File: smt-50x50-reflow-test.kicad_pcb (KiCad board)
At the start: 4 copper layers, 0 parts

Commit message: pcb: fix missing 3d models
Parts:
- added AE1: Antenna, RF_Antenna:Johanson_2450AT18x100, F.Cu at (162.5, 82.0)
- added C1: 1u, Capacitor_SMD:C_0603_1608Metric, F.Cu at (128.3, 74.4)
- added C10: 0u1, Capacitor_SMD:C_0402_1005Metric, F.Cu at (127.7, 95.6)
- added C11: 0u1, Capacitor_SMD:C_0402_1005Metric, F.Cu at (127.7, 97.6)
- added C12: 0u1, Capacitor_SMD:C_0402_1005Metric, F.Cu at (127.7, 99.5)
- added C13: 10n, Capacitor_SMD:C_0402_1005Metric, F.Cu at (127.7, 101.5)
- added C14: 1u, Capacitor_SMD:C_0402_1005Metric, F.Cu at (130.6, 91.7)
- added C15: 1u, Capacitor_SMD:C_0402_1005Metric, F.Cu at (130.6, 93.6)
- added C16: 0u1, Capacitor_SMD:C_0402_1005Metric, F.Cu at (130.6, 95.6)
- added C17: 0u1, Capacitor_SMD:C_0402_1005Metric, F.Cu at (130.6, 97.6)
- added C18: 0u1, Capacitor_SMD:C_0402_1005Metric, F.Cu at (130.6, 99.5)
- added C19: 1u, Capacitor_SMD:C_0402_1005Metric, F.Cu at (130.6, 101.5)
- added C2: 1u, Capacitor_SMD:C_0603_1608Metric, F.Cu at (128.3, 76.9)
- added C20: 10u, Capacitor_SMD:C_0402_1005Metric, F.Cu at (133.5, 91.7)
- added C21: 22u, Capacitor_SMD:C_0603_1608Metric, F.Cu at (128.3, 84.4)
- added C22: 1u, Capacitor_SMD:C_0402_1005Metric, F.Cu at (133.5, 93.6)
- added C23: 12p, Capacitor_SMD:C_0402_1005Metric, F.Cu at (133.5, 95.6)
- added C25: 12p, Capacitor_SMD:C_0402_1005Metric, F.Cu at (133.5, 97.6)
- added C28: 1p2, Capacitor_SMD:C_0402_1005Metric, F.Cu at (133.5, 99.5)
- added C29: 1p2, Capacitor_SMD:C_0402_1005Metric, F.Cu at (133.5, 101.5)
- added C4: 0u1, Capacitor_SMD:C_0603_1608Metric, F.Cu at (128.3, 79.4)
- added C48: 0u1, Capacitor_SMD:C_0402_1005Metric, F.Cu at (136.4, 91.7)
- added C49: 0u1, Capacitor_SMD:C_0402_1005Metric, F.Cu at (136.4, 93.6)
- added C5: 1u, Capacitor_SMD:C_0603_1608Metric, F.Cu at (128.3, 81.9)
- added C50: 0u1, Capacitor_SMD:C_0402_1005Metric, F.Cu at (136.4, 95.6)
- added C51: 0u1, Capacitor_SMD:C_0402_1005Metric, F.Cu at (136.4, 97.6)
- added C52: 1p, Capacitor_SMD:C_0402_1005Metric, F.Cu at (136.4, 99.5)
- added C6: 4u7, Capacitor_SMD:C_1206_3216Metric, F.Cu at (141.2, 109.2)
- added C7: 4u7, Capacitor_SMD:C_1206_3216Metric, F.Cu at (141.2, 112.5)
- added C8: 10u, Capacitor_SMD:C_0402_1005Metric, F.Cu at (127.7, 91.7)
- added C9: 1u, Capacitor_SMD:C_0402_1005Metric, F.Cu at (127.7, 93.6)
- added D1: RED, LED_SMD:LED_0603_1608Metric, F.Cu at (165.8, 110.0)
- added D2: GREEN, LED_SMD:LED_0805_2012Metric, F.Cu at (160.9, 112.2)
- added D3: H5VU10U, Pers:Diode_DFN1006, F.Cu at (152.8, 82.3)
- added D5: WHITE, LED_SMD:LED_0603_1608Metric, F.Cu at (165.8, 112.6)
- added D7: D_Schottky, Diode_SMD:D_SMA, F.Cu at (142.4, 105.2)
- added J1: Conn_01x04_Pin, Connector_PinHeader_2.54mm:PinHeader_1x04_P2.54mm_Vertical, F.Cu at (140.6, 75.4)
- added J2: Conn_01x02, Connector_PinHeader_2.54mm:PinHeader_1x02_P2.54mm_Vertical, F.Cu at (162.0, 75.4)
- added J4: USB_C_Receptacle_USB2.0_14P, Connector_USB:USB_C_Receptacle_HRO_TYPE-C-31-M-12, F.Cu at (132.2, 108.3)
- added J8: Conn_01x04_Pin, Connector_PinHeader_2.54mm:PinHeader_1x04_P2.54mm_Vertical, F.Cu at (145.2, 75.4)
- added J9: Conn_01x03_Pin, Connector_PinHeader_2.54mm:PinHeader_1x03_P2.54mm_Vertical, F.Cu at (140.6, 95.6)
- added JP2: Jumper_3_Bridged12, Connector_PinHeader_2.54mm:PinHeader_1x03_P2.54mm_Vertical, F.Cu at (145.2, 95.6)
- added L1: 33u, Inductor_SMD:L_Chilisin_BMRx00060630, F.Cu at (152.5, 97.3)
- added L2: 2n7, Inductor_SMD:L_0402_1005Metric, F.Cu at (139.8, 86.3)
- added L3: 24n, Inductor_SMD:L_0402_1005Metric, F.Cu at (139.8, 88.3)
- added L4: 2n7, Inductor_SMD:L_0402_1005Metric, F.Cu at (139.8, 90.3)
- added L6: 3n9, Inductor_SMD:L_0402_1005Metric, F.Cu at (139.8, 92.3)
- added L7: 2n7, Inductor_SMD:L_0402_1005Metric, F.Cu at (142.7, 86.3)
- added R1: 0, Resistor_SMD:R_0402_1005Metric, F.Cu at (142.7, 88.3)
- added R10: 22, Resistor_SMD:R_0402_1005Metric, F.Cu at (148.5, 88.3)
- added R11: 5k1, Resistor_SMD:R_0603_1608Metric, F.Cu at (128.3, 89.4)
- added R12: 5k1, Resistor_SMD:R_0603_1608Metric, F.Cu at (132.3, 74.4)
- added R13: 5k1, Resistor_SMD:R_0603_1608Metric, F.Cu at (132.3, 76.9)
- added R14: 22, Resistor_SMD:R_0402_1005Metric, F.Cu at (148.5, 90.3)
- added R15: 5k1, Resistor_SMD:R_0603_1608Metric, F.Cu at (132.3, 79.4)
- added R16: 470, Resistor_SMD:R_0402_1005Metric, F.Cu at (148.5, 92.3)
- added R2: 0, Resistor_SMD:R_0402_1005Metric, F.Cu at (142.7, 90.3)
- added R29: 15k, Resistor_SMD:R_0603_1608Metric, F.Cu at (132.3, 81.9)
- added R3: 0, Resistor_SMD:R_0402_1005Metric, F.Cu at (142.7, 92.3)
- added R30: 9k1, Resistor_SMD:R_0603_1608Metric, F.Cu at (132.3, 84.4)
- added R31: 5k1, Resistor_SMD:R_0603_1608Metric, F.Cu at (132.3, 86.9)
- added R32: 100k, Resistor_SMD:R_0603_1608Metric, F.Cu at (132.3, 89.4)
- added R33: 40k, Resistor_SMD:R_0603_1608Metric, F.Cu at (136.3, 74.4)
- added R4: 0, Resistor_SMD:R_0402_1005Metric, F.Cu at (145.6, 86.3)
- added R5: 0, Resistor_SMD:R_0402_1005Metric, F.Cu at (145.6, 88.3)
- added R57: 10k, Resistor_SMD:R_0603_1608Metric, F.Cu at (136.3, 76.9)
- added R58: 10k, Resistor_SMD:R_0603_1608Metric, F.Cu at (136.3, 79.4)
- added R6: 0, Resistor_SMD:R_0402_1005Metric, F.Cu at (145.6, 90.3)
- added R62: 10k, Resistor_SMD:R_0603_1608Metric, F.Cu at (136.3, 81.9)
- added R7: 10k, Resistor_SMD:R_0402_1005Metric, F.Cu at (145.6, 92.3)
- added R8: 10k, Resistor_SMD:R_0402_1005Metric, F.Cu at (148.5, 86.3)
- added R9: 10k, Resistor_SMD:R_0603_1608Metric, F.Cu at (128.3, 86.9)
- added SW1: SW_Push, Button_Switch_SMD:SW_SPST_TS-1088-xR020, F.Cu at (155.1, 103.7)
- added SW2: SW_Push, Button_Switch_SMD:SW_SPST_TS-1088-xR020, F.Cu at (155.1, 108.2)
- added TP13: TestPoint, TestPoint:TestPoint_Pad_D2.0mm, F.Cu at (149.5, 103.5)
- added TP15: TestPoint, TestPoint:TestPoint_Pad_D2.0mm, F.Cu at (149.5, 107.5)
- added TP17: TestPoint, TestPoint:TestPoint_Pad_D2.0mm, F.Cu at (149.5, 111.5)
- added U1: ESP32-C6, Package_DFN_QFN:QFN-40-1EP_5x5mm_P0.4mm_EP3.6x3.6mm_ThermalVias, F.Cu at (163.4, 88.9)
- added U14: TMP117AIDRV, Package_SON:WSON-6-1EP_2x2mm_P0.65mm_EP1x1.6mm, F.Cu at (165.6, 103.3)
- added U15: BMP581, Pers:Bosch_LGA-10_2x2mm_P0.8mm_AntiClockwisePinNumbering, F.Cu at (149.3, 83.2)
- added U16: TMP117AIDRV, Package_SON:WSON-6-1EP_2x2mm_P0.65mm_EP1x1.6mm, F.Cu at (165.6, 106.9)
- added U2: W25Q128JVS, Package_SO:SOIC-8_5.3x5.3mm_P1.27mm, F.Cu at (162.6, 96.8)
- added U3: AP2112K-3.3, Package_TO_SOT_SMD:SOT-23-5, F.Cu at (161.2, 103.8)
- added U4: LM317_TO-252, Package_TO_SOT_SMD:TO-252-2, F.Cu at (154.4, 77.3)
- added U5: LMR36520FADDA, Package_SO:Texas_HTSOP-8-1EP_3.9x4.9mm_P1.27mm_EP2.95x4.9mm_Mask2.4x3.1mm_ThermalVias, F.Cu at (154.7, 88.7)
- added U7: USBLC6-2SC6, Package_TO_SOT_SMD:SOT-23-6, F.Cu at (161.2, 108.5)
- added Y1: 48M, Crystal:Crystal_SMD_2016-4Pin_2.0x1.6mm, F.Cu at (153.6, 112.3)

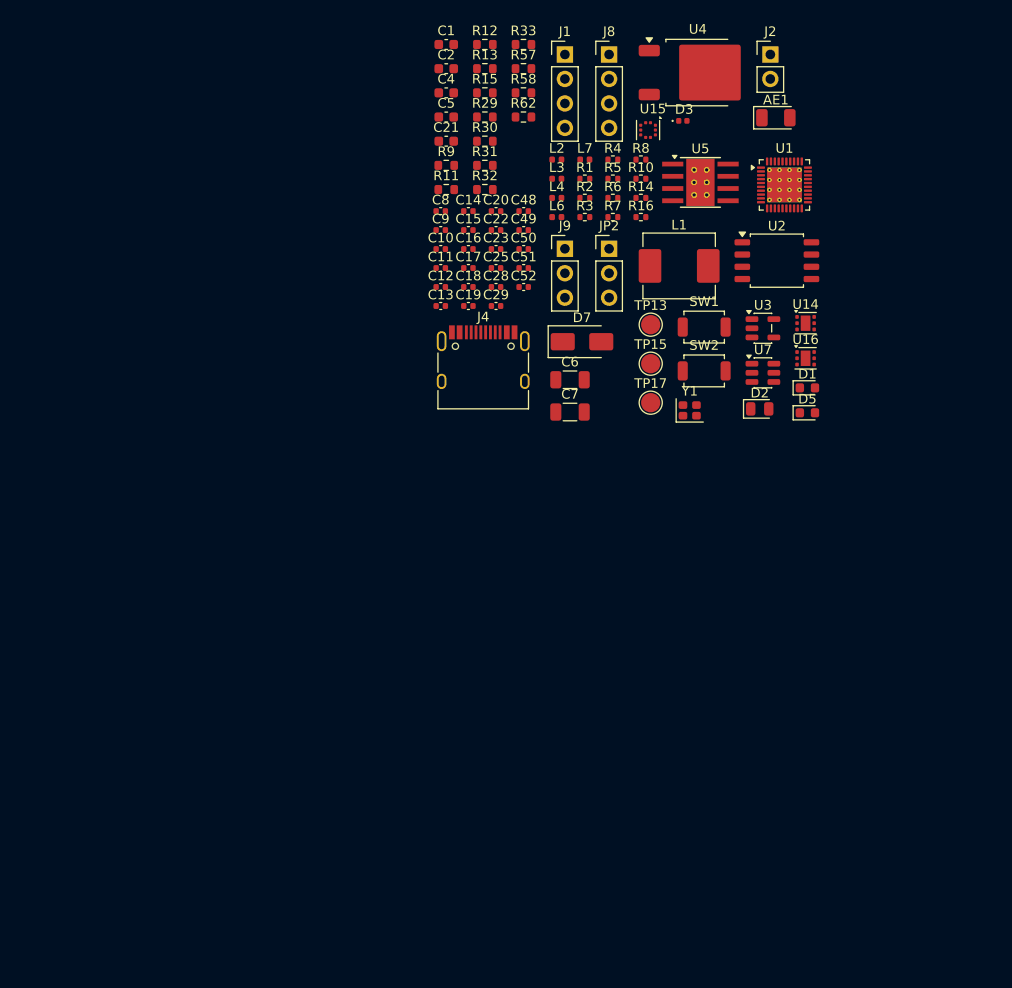
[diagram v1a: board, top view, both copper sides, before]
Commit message: pcb: add board outline
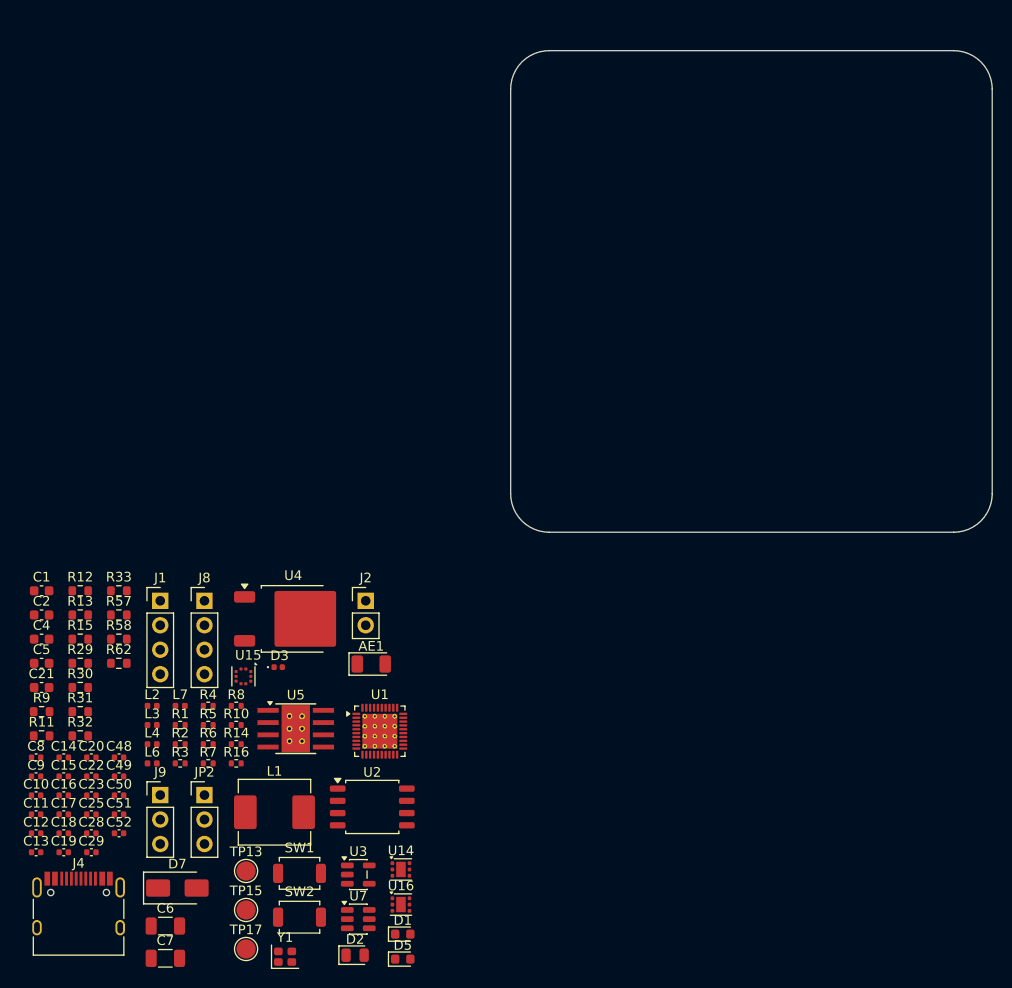
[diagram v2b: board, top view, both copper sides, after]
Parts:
- moved C14 70.6 mm to (88.6, 148.4)
- moved C15 70.6 mm to (88.6, 150.3)
- moved C16 70.6 mm to (88.6, 152.3)
- moved C17 70.6 mm to (88.6, 154.3)
- moved D2 70.6 mm to (118.8, 168.9)
- moved R33 70.6 mm to (94.3, 131.1)
- moved R4 70.6 mm to (103.6, 143.0)
- moved R5 70.6 mm to (103.6, 145.0)
- moved R57 70.6 mm to (94.3, 133.6)
- moved R58 70.6 mm to (94.3, 136.1)
- moved R62 70.6 mm to (94.3, 138.6)
- moved R7 70.6 mm to (103.6, 149.0)
- moved U15 70.6 mm to (107.3, 140.0)
- moved U2 70.6 mm to (120.6, 153.5)
- moved C1 70.6 mm to (86.3, 131.1)
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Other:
- board outline added: 50 x 50 mm

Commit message: pcb: add M2 mounting holes
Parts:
- added REF**: MountingHole_2.2mm_M2_Pad_Via, MountingHole:MountingHole_2.2mm_M2_Pad_Via, F.Cu at (139.0, 121.0)
- added REF**: MountingHole_2.2mm_M2_Pad_Via, MountingHole:MountingHole_2.2mm_M2_Pad_Via, F.Cu at (181.0, 121.0)
- added REF**: MountingHole_2.2mm_M2_Pad_Via, MountingHole:MountingHole_2.2mm_M2_Pad_Via, F.Cu at (181.0, 79.0)
- added REF**: MountingHole_2.2mm_M2_Pad_Via, MountingHole:MountingHole_2.2mm_M2_Pad_Via, F.Cu at (139.0, 79.0)

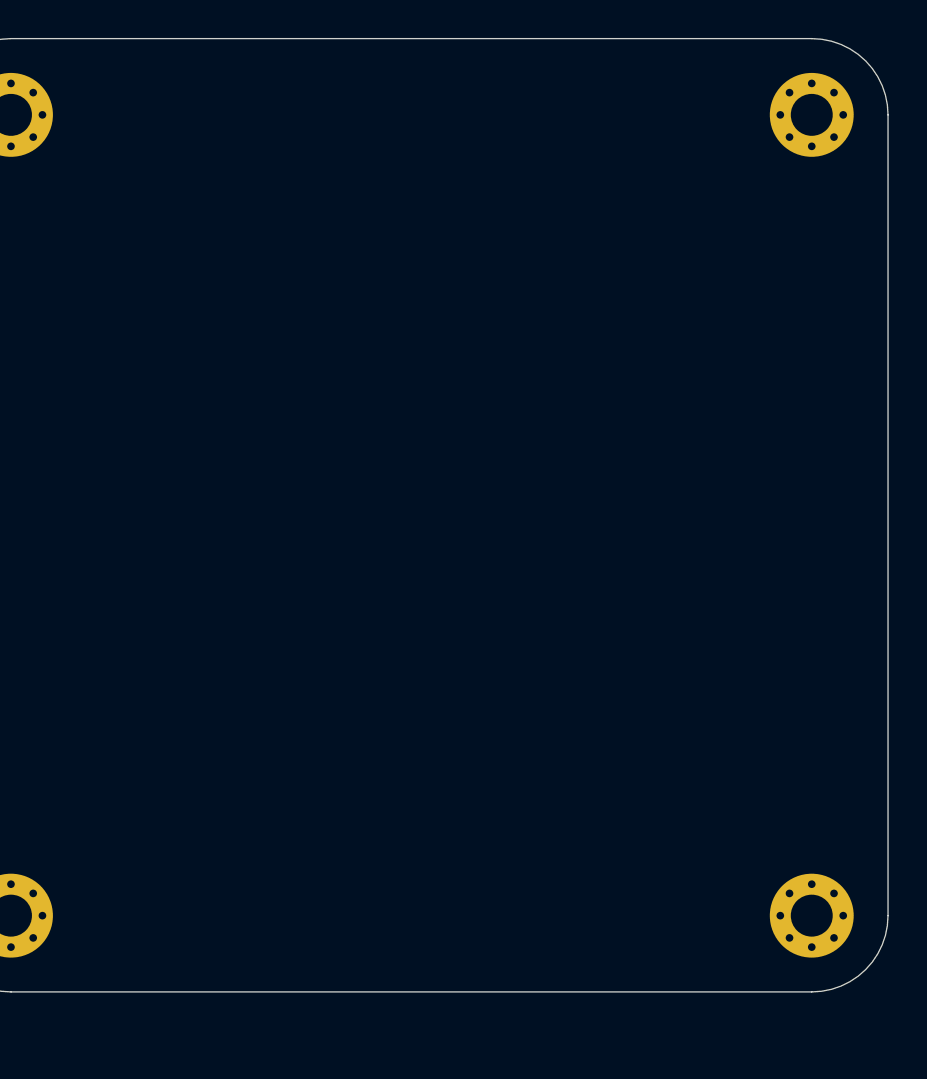
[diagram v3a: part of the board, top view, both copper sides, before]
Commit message: pcb: add M2 tooling holes
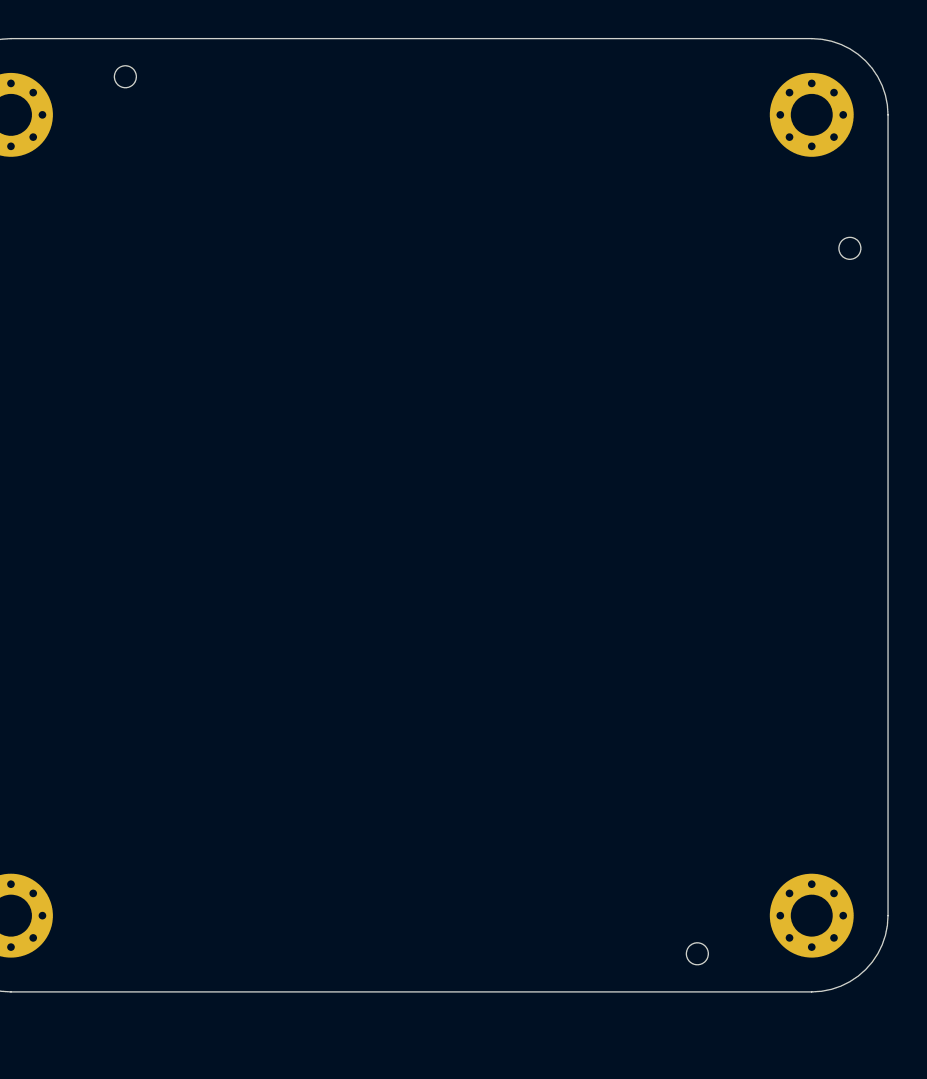
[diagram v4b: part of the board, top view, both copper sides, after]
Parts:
- added REF**: ToolingHole_1.152mm, MountingHole:ToolingHole_1.152mm, F.Cu at (175.0, 123.0)
- added REF**: ToolingHole_1.152mm, MountingHole:ToolingHole_1.152mm, F.Cu at (145.0, 77.0)
- added REF**: ToolingHole_1.152mm, MountingHole:ToolingHole_1.152mm, F.Cu at (183.0, 86.0)

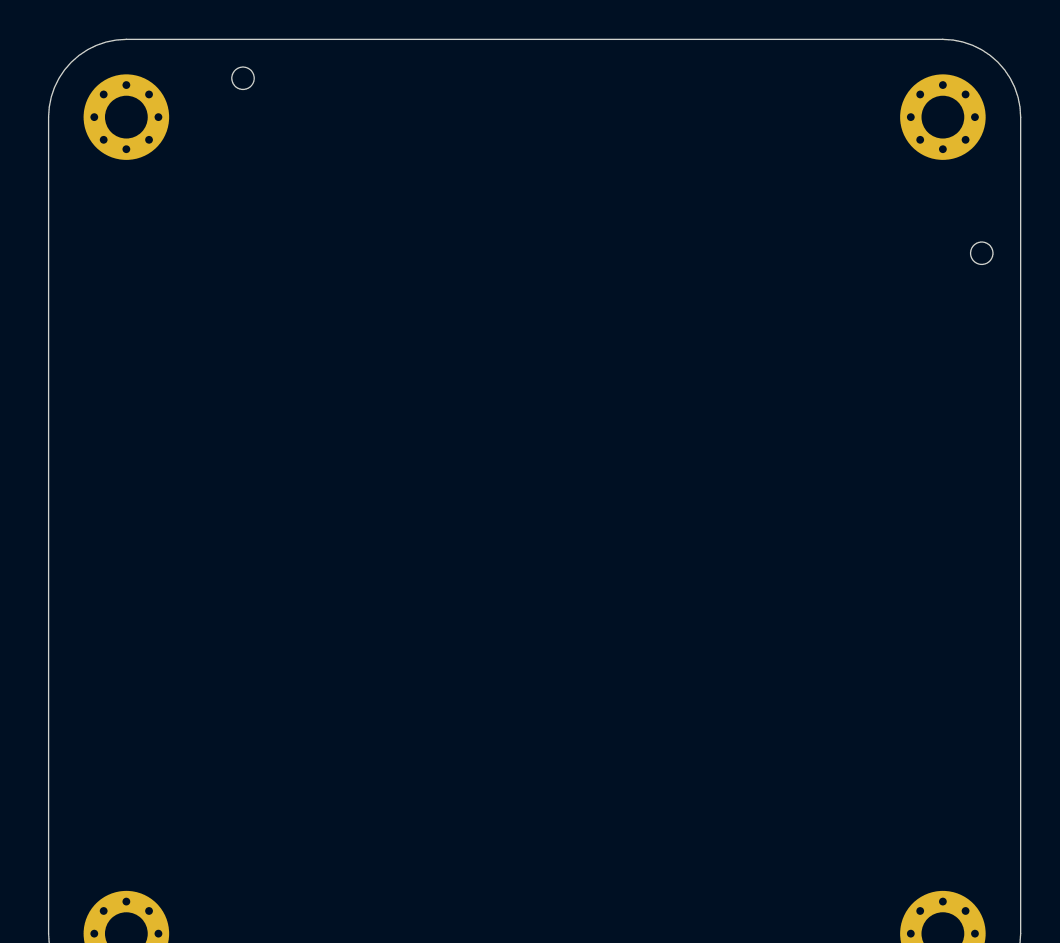
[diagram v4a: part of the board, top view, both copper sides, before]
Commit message: pcb: add fiducials
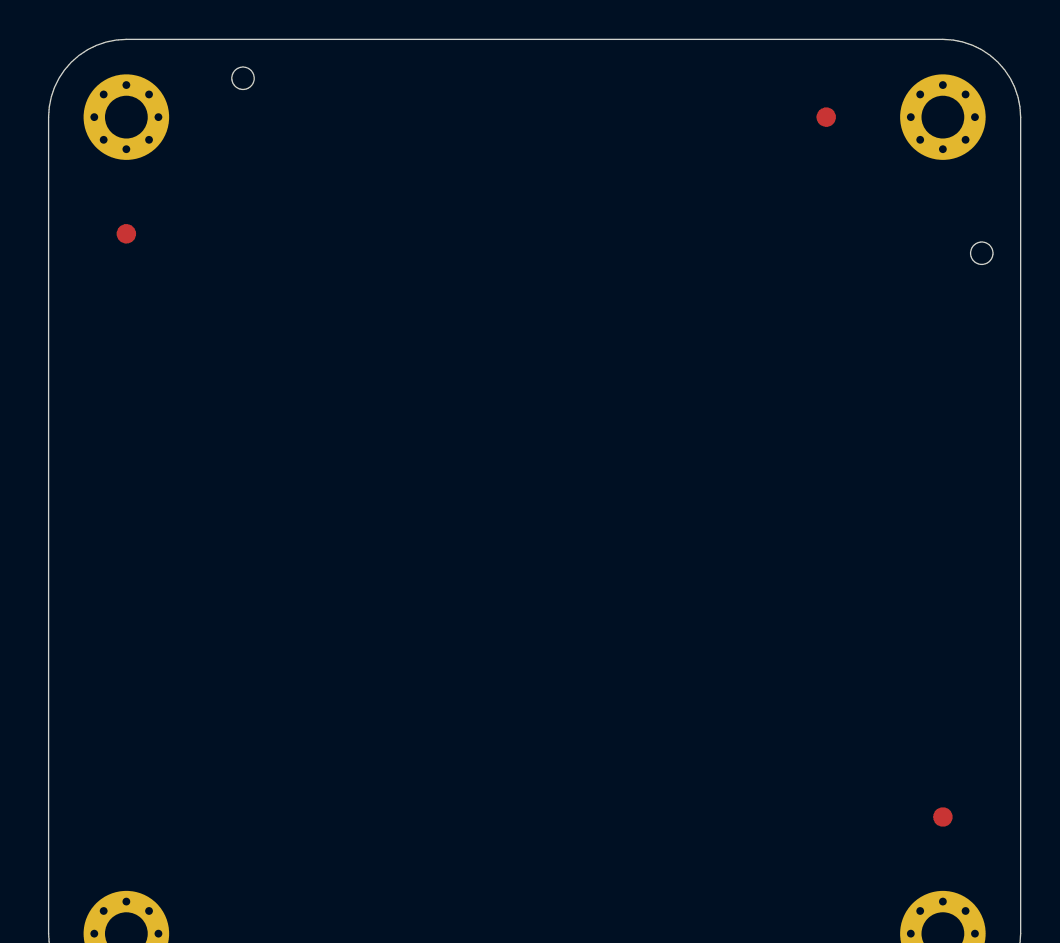
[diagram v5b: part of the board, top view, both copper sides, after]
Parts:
- added REF**: Fiducial_1mm_Mask2mm, Fiducial:Fiducial_1mm_Mask2mm, F.Cu at (181.0, 115.0)
- added REF**: Fiducial_1mm_Mask2mm, Fiducial:Fiducial_1mm_Mask2mm, F.Cu at (175.0, 79.0)
- added REF**: Fiducial_1mm_Mask2mm, Fiducial:Fiducial_1mm_Mask2mm, F.Cu at (139.0, 85.0)
